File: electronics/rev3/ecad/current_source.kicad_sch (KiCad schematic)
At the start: 19 parts, among them Q25 2N3906, U2 LM4030-2.5, U3 OPA4388IDR, U6 CD4066BM

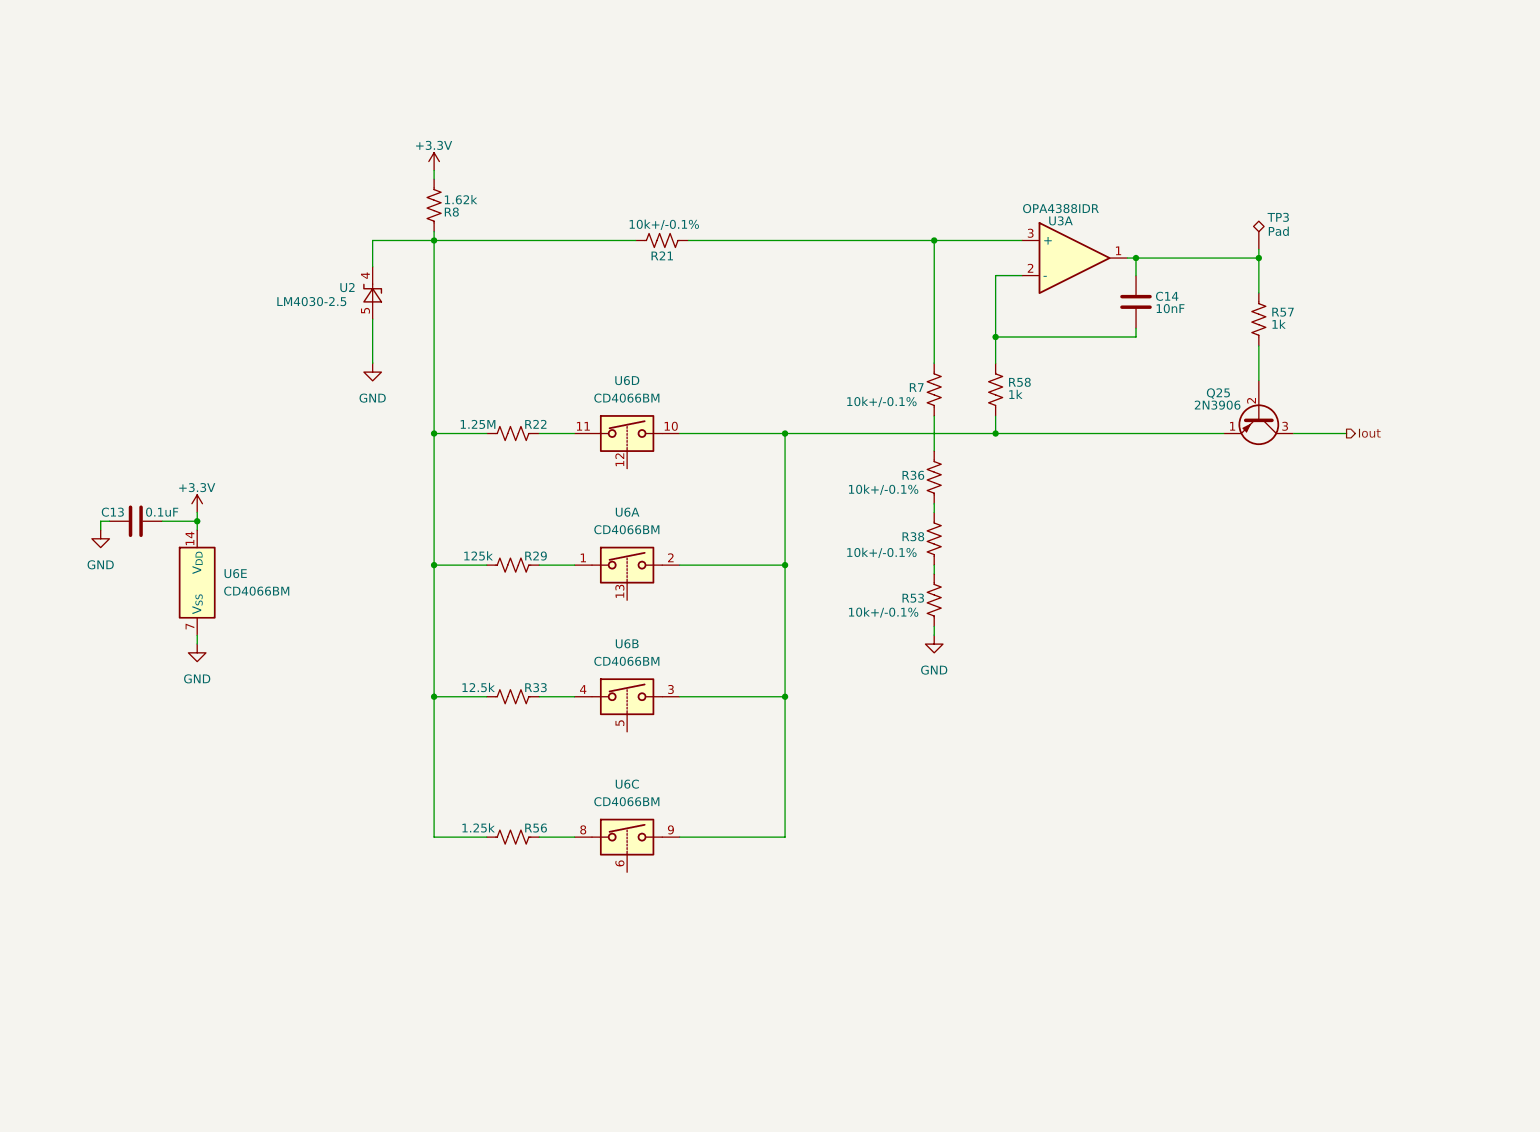
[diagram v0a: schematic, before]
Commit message: rev3 schematic work
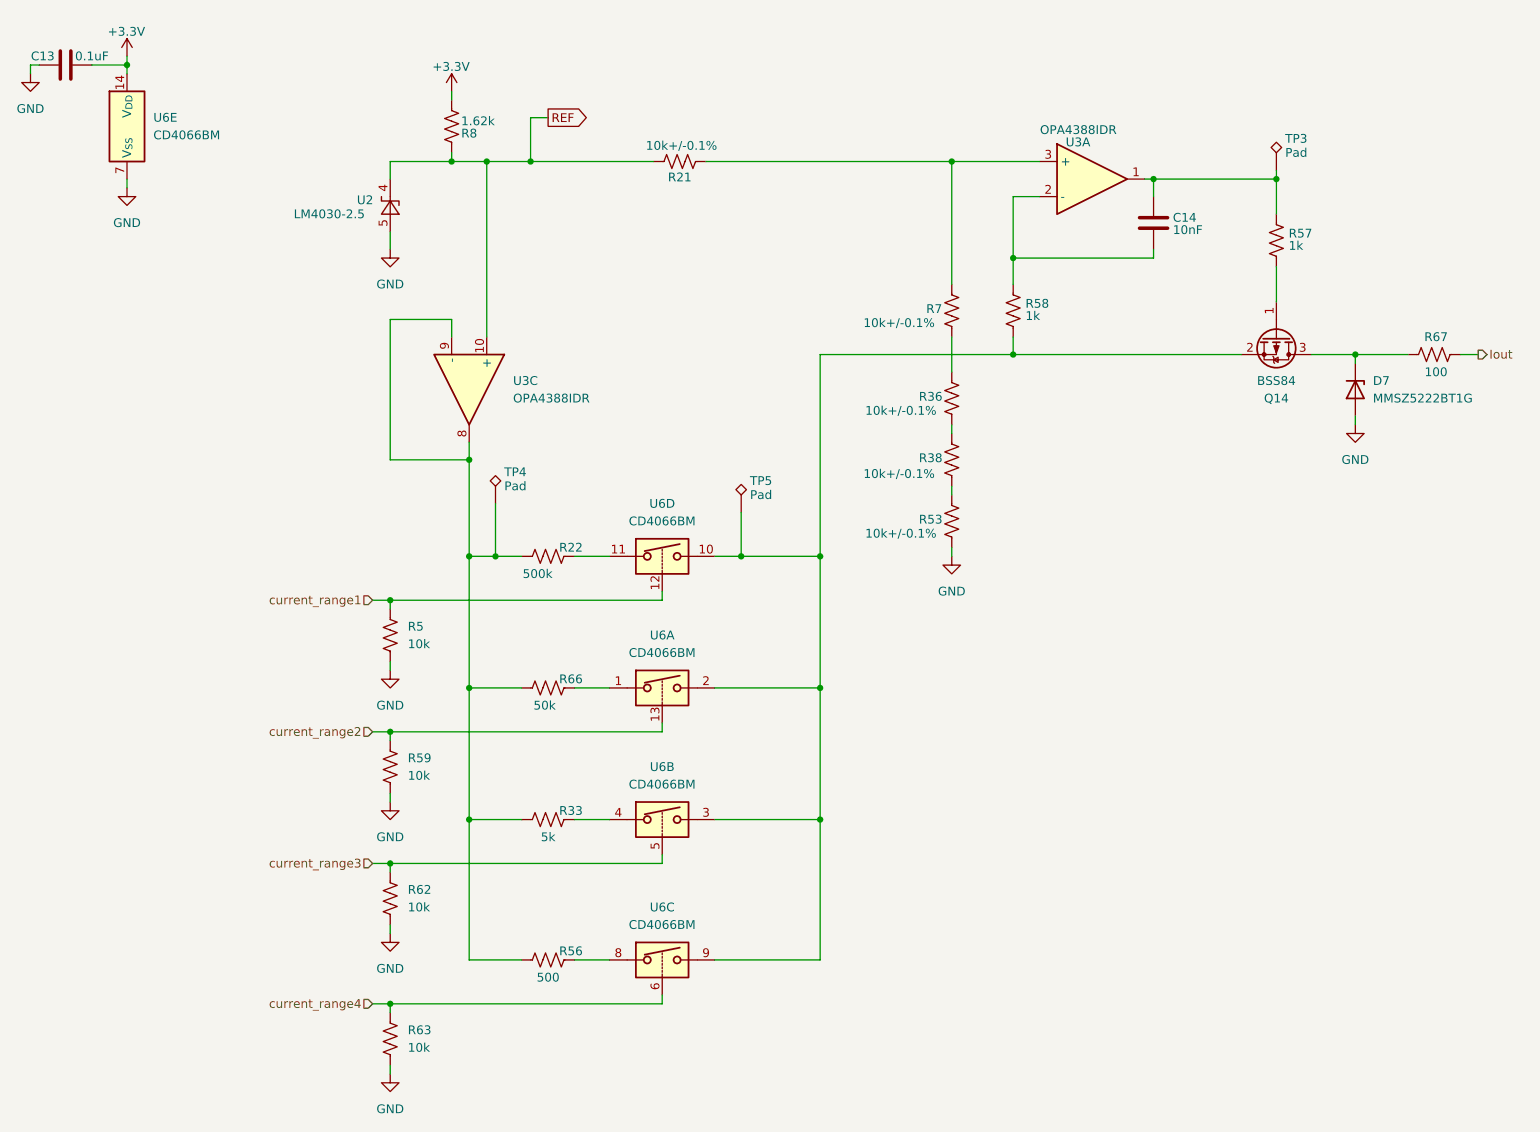
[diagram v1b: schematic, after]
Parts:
- removed Q25: 2N3906, Package_TO_SOT_THT:TO-92_Inline, symbol Transistor_BJT:2N3906
- removed R29: 125k, symbol Device:R_US
- added D7: MMSZ5222BT1G, symbol Device:D_Zener
- added Q14: BSS84, Package_TO_SOT_SMD:SOT-23, symbol Transistor_FET:BSS84
- added R5: 10k, symbol Device:R_US
- added R59, R62, R63: 10k, Resistor_SMD:R_0805_2012Metric, symbol Device:R_US
- added R66: 50k, Resistor_SMD:R_0805_2012Metric, symbol Device:R_US
- added R67: 100, Resistor_SMD:R_0805_2012Metric, symbol Device:R_US
- added TP4, TP5: Pad, TestPoint:TestPoint_THTPad_1.5x1.5mm_Drill0.7mm, symbol Connector:TestPoint_Alt
- added unit 3 of U3
- C13, C14: footprint (none) -> Capacitor_SMD:C_0805_2012Metric
- R22: value 1.25M -> 500k
- R33: value 12.5k -> 5k
- R53, R57, R58: footprint (none) -> Resistor_SMD:R_0805_2012Metric
- R56: value 1.25k -> 500; footprint (none) -> Resistor_SMD:R_0805_2012Metric
- U3: footprint Package_SO:SOIC-14_3.9x8.7mm_P1.27mm -> (none); Digikey Part # 296-53511-1-ND -> (none); Part # OPA4388IDR -> (none); Unit Price 4.92 -> (none)
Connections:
- net GND: now also D7.2 (A), R5.2, R59.2, R62.2, R63.2
- net Iout: now also R67.2
- net current_range4: now reaches U6.6
- net current_range4: now also R63.1
- net at R58.2, U6.10, U6.2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: now also Q14.2 (S), TP5.1
- net at R57.2: now also Q14.1 (G)
- net at R22.1, R33.1, R56.1: now also R66.1, TP4.1, U3.8, U3.9 (-); no longer R21.1, R8.2, U2.4 (K)
- net current_range1: now reaches U6.12
- net current_range1: now also R5.1
- net at U6.1: now also R66.2
- net current_range2: now reaches U6.13
- net current_range2: now also R59.1
- net current_range3: now reaches U6.5
- net current_range3: now also R62.1
- new net: D7.1 (K), Q14.3 (D), R67.1
- new net REF: R21.1, R8.2, U2.4 (K), U3.10 (+)
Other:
- title: (none) -> Current Source
- moved on the sheet: C13, C14, R21, R22, R33, R36, R38, R53, R56, R57, R58, R7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

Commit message: layout work rev3
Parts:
- removed D7: MMSZ5222BT1G, symbol Device:D_Zener
- removed R67: 100, Resistor_SMD:R_0805_2012Metric, symbol Device:R_US
- removed U6: CD4066BM, Package_SO:SO-14_3.9x8.65mm_P1.27mm, symbol Analog_Switch:CD4066BM
- added D7: BAT46W-7-F, Diode_SMD:D_SOD-123, symbol Device:D_Schottky
- added U5: TS3A4751PWR, Package_SO:TSSOP-14_4.4x5mm_P0.65mm, symbol multimeter_parts:TS3A4751PWR
- R21, R22, R33, R36, R38, R5, R7: footprint (none) -> Resistor_SMD:R_0805_2012Metric
- R8: footprint Resistor_SMD:R_0805_2012Metric_Pad1.20x1.40mm_HandSolder -> Resistor_SMD:R_0805_2012Metric
- U3: footprint (none) -> Package_SO:SOIC-14_3.9x8.7mm_P1.27mm
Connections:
- net +3.3V: now also U5.14 (VCC)
- net GND: now also U5.7 (GND)
- net Iout: now also D7.1 (K)
- net current_range1: now also U5.13 (IN1)
- net current_range2: now also U5.5 (IN2)
- net current_range3: now also U5.6 (IN3)
- net current_range4: now also U5.12 (IN4)
- net at R56.2: now also U5.10 (COM4)
- net at Q14.2 (S), R58.2, TP5.1: now also U5.1 (NO1), U5.11 (NO4), U5.3 (NO2), U5.8 (NO3)
- net at Q14.3 (D): now also D7.2 (A)
- net at R22.2: now also U5.2 (COM1)
- net at R66.2: now also U5.4 (COM2)
- net at R33.2: now also U5.9 (COM3)
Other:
- note added: "Rmax=200k"
- note added: "Rmax=20k"
- note added: "Rmax=2M"
- note added: "Rmax=2k"
- moved on the sheet: C13, C14, Q14, R21, R22, R33, R36, R38, R5, R53, R56, R57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

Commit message: layout complete
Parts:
- C13: Digikey Part # (none) -> 1276-1003-1-ND; Part # (none) -> CL21B104KBCNNNC; Unit Price (none) -> 0.1
- Q14: Digikey Part # (none) -> BSS84CT-ND; Part # (none) -> BSS84; Unit Price (none) -> 0.48
- R21, R36, R38, R53, R7: Digikey Part # (none) -> P10KDACT-ND; Part # (none) -> ERA-6AEB103V; Unit Price (none) -> 0.13
- R5, R59, R62, R63: Digikey Part # (none) -> RMCF0805FT10K0CT-ND; Part # (none) -> RMCF0805FT10K0; Unit Price (none) -> 0.1

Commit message: rev3 work
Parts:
- R57, R58: Digikey Part # (none) -> RMCF0805FT1K00CT-ND; Part # (none) -> RMCF0805FT1K00; Unit Price (none) -> 0.1
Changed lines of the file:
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@@
+			)
+		)
+		(property "Digikey Part #" "RMCF0805FT1K00CT-ND"
+			(at 163.83 54.61 0)
+			(effects
+				(font
+					(size 1.27 1.27)
+				)
+				(hide yes)
+			)
+		)
+		(property "Part #" "RMCF0805FT1K00"
+			(at 163.83 54.61 0)
+			(effects
+				(font
+					(size 1.27 1.27)
+				)
+				(hide yes)
+			)
+		)
+		(property "Unit Price" "0.1"
+			(at 163.83 54.61 0)
+			(effects
+				(font
+					(size 1.27 1.27)
+				)
+				(hide yes)
 			)
 		)
@@
 			(at 201.93 44.45 0)
 			(effects
+				(font
+					(size 1.27 1.27)
+				)
+				(hide yes)
+			)
+		)
+		(property "Digikey Part #" "RMCF0805FT1K00CT-ND"
+			(at 201.93 44.45 0)
+			(effects
+				(font
+					(size 1.27 1.27)
+				)
+				(hide yes)
+			)
+		)
+		(property "Part #" "RMCF0805FT1K00"
+			(at 201.93 44.45 0)
+			(effects
+				(font
+					(size 1.27 1.27)
+				)
+				(hide yes)
+			)
+		)
+		(property "Unit Price" "0.1"
+			(at 201.93 44.45 0)
+			(effects

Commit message: BOM
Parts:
- C14: Digikey Part # (none) -> 399-C0805C103K5RACTUCT-ND; Part # (none) -> C0805C103K5RACTU; Unit Price (none) -> 0.08
- D7: Digikey Part # (none) -> BAT46W-7FDICT-ND; Part # (none) -> BAT46W-7-F; Unit Price (none) -> 0.2
- R22: value 500k -> 500k+/-0.1%; Digikey Part # (none) -> 738-RNCF0805BTE500KCT-ND; Part # (none) -> RNCF0805BTE500K; Unit Price (none) -> 0.12
- R33: value 5k -> 5k+/-0.1%; Digikey Part # (none) -> PNM0805-5.0KBCT-ND; Part # (none) -> PNM0805E5001BST5; Unit Price (none) -> 0.8
- R56: value 500 -> 499+/-0.1%; Digikey Part # (none) -> RG20P499KBCT-ND; Part # (none) -> RG2012P-4993-B-T5; Unit Price (none) -> 0.1
- R66: value 50k -> 50k+/-0.1%; Digikey Part # (none) -> 749-MCU08050D5002BP100CT-ND; Part # (none) -> MCU08050D5002BP100; Unit Price (none) -> 0.57
- U3: Digikey Part # (none) -> 296-53511-1-ND; Part # (none) -> OPA4388IDR; Unit Price (none) -> 4.92
- U5: Digikey Part # (none) -> 296-20700-1-ND; Part # (none) -> TS3A4751PWR; Unit Price (none) -> 1.62
